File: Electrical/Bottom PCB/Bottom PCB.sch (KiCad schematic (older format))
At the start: 47 parts, among them J101 Steper1, J102 Steper2, J103 H Bridge, J104 Servo1, J105 Servo2, J106 Servo3, J107 Servo4, SW101 FL, SW102 FR, U101 ULN2003A, U102 74HC595, U103 QRE1113, U104 TB6612FNG, U105 74HC595, U106 QRE1113, U107 QRE1113, U108 MCP23017_SO, U109 QRE1113

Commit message: simplified the pcb,
Removed the shift registers and moved functionality onto the 16 way IO expander, also removed the H-Bridge, may re-add a I2C duel h-bridge at a later date.

Thinking about best way to drive the four servo headers, may use I2C controller for them as well, as then the timing maths is removed from the main micro
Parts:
- removed C105, C108: 100pF, Capacitor_SMD:C_1206_3216Metric_Pad1.42x1.75mm_HandSolder, symbol Device:C_Small
- removed C106: 10uF, Capacitor_SMD:C_1206_3216Metric_Pad1.42x1.75mm_HandSolder, symbol Device:C_Small
- removed J103: H Bridge, Connector_PinHeader_2.54mm:PinHeader_1x04_P2.54mm_Vertical, symbol Connector_Generic:Conn_01x04
- removed U102, U105: 74HC595, Package_SO:SOIC-16W_5.3x10.2mm_P1.27mm, symbol 74xx:74HC595
- removed U104: TB6612FNG, Package_SO:SSOP-24_5.3x8.2mm_P0.65mm, symbol Driver_Motor:TB6612FNG
- C102: value 100pF -> 10uF
- JP101, JP102, JP103: renamed from JP?; footprint (none) -> Jumper:SolderJumper-2_P1.3mm_Open_Pad1.0x1.5mm
- gave numbers to parts that had none: 3
- renumbered R109 to R112, R110 to R113, U108 to U107, U107 to U108
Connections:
- net labels removed: DATA, M1PWM, M2PWM, RCLK, SRCLK
- wire segments 262 -> 178
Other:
- moved on the sheet: C101, C102, C103, C104, J101, J102, JP101, JP102, JP103, R109, R110, R111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

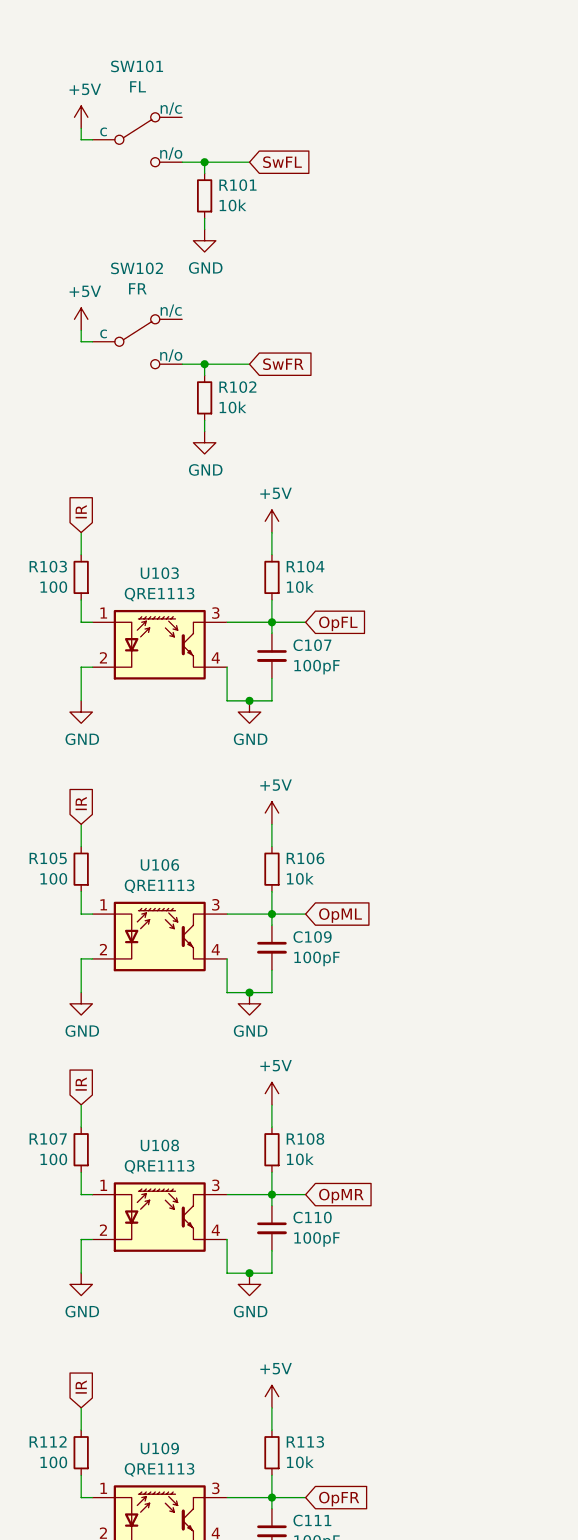
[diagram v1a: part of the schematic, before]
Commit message: moved some parts to 5V supply
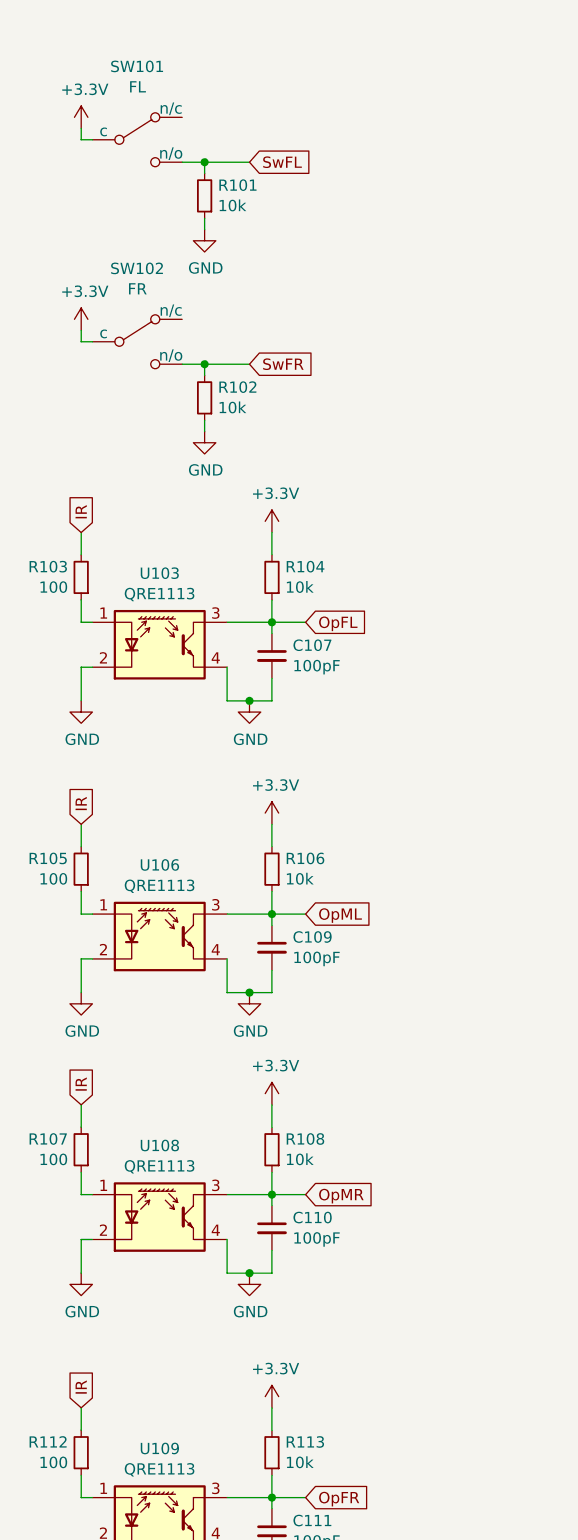
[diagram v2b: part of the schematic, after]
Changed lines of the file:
@@
-	1    0    0    -1
-$EndComp
-$Comp
-L power:+5V #PWR0115
-U 1 1 5DA4321E
-P 550 1650
-F 0 "#PWR0115" H 550 1500 50  0001 C CNN
-F 1 "+5V" H 565 1823 50  0000 C CNN
-F 2 "" H 550 1650 50  0001 C CNN
-F 3 "" H 550 1650 50  0001 C CNN
-	1    550  1650
 	1    0    0    -1
 $EndComp
@@
 F 3 "" H 1100 1200 50  0001 C CNN
 	1    1100 1200
-	1    0    0    -1
-$EndComp
-$Comp
-L power:+5V #PWR0106
-U 1 1 5DA58E34
-P 550 750
-F 0 "#PWR0106" H 550 600 50  0001 C CNN
-F 1 "+5V" H 565 923 50  0000 C CNN
-F 2 "" H 550 750 50  0001 C CNN
-F 3 "" H 550 750 50  0001 C CNN
-	1    550  750
 	1    0    0    -1
 $EndComp
@@
 	1    0    0    -1
 $EndComp
-$Comp
-L power:+5V #PWR0127
-U 1 1 5E63ABEC
-P 1400 2550
-F 0 "#PWR0127" H 1400 2400 50  0001 C CNN
-F 1 "+5V" H 1415 2723 50  0000 C CNN
-F 2 "" H 1400 2550 50  0001 C CNN
-F 3 "" H 1400 2550 50  0001 C CNN
-	1    1400 2550
-	1    0    0    -1
-$EndComp
 Wire Wire Line
 	550  2850 550  2950
@@
 	1    0    0    -1
 $EndComp
-$Comp
-L power:+5V #PWR0134
-U 1 1 5E7C0801
-P 1400 3850
-F 0 "#PWR0134" H 1400 3700 50  0001 C CNN
-F 1 "+5V" H 1415 4023 50  0000 C CNN
-F 2 "" H 1400 3850 50  0001 C CNN
-F 3 "" H 1400 3850 50  0001 C CNN
-	1    1400 3850
-	1    0    0    -1
-$EndComp
 Wire Wire Line
 	550  4150 550  4250
@@
 	1    0    0    -1
 $EndComp
-$Comp
-L power:+5V #PWR0145
-U 1 1 5E7D8F2B
-P 1400 5100
-F 0 "#PWR0145" H 1400 4950 50  0001 C CNN
-F 1 "+5V" H 1415 5273 50  0000 C CNN
-F 2 "" H 1400 5100 50  0001 C CNN
-F 3 "" H 1400 5100 50  0001 C CNN
-	1    1400 5100
-	1    0    0    -1
-$EndComp
 Wire Wire Line
 	550  5400 550  5500
@@
 Wire Wire Line
 	550  6750 550  6850
-$Comp
-L power:+5V #PWR0149
-U 1 1 5E7513F0
-P 1400 6450
-F 0 "#PWR0149" H 1400 6300 50  0001 C CNN
-F 1 "+5V" H 1415 6623 50  0000 C CNN
-F 2 "" H 1400 6450 50  0001 C CNN
-F 3 "" H 1400 6450 50  0001 C CNN
-	1    1400 6450
-	1    0    0    -1
-$EndComp
 $Comp
 L Device:C_Small C111
@@
 	5200 2400 5650 2400
 $Comp
-L power:+5V #PWR?
+L power:+5V #PWR0102
 U 1 1 5EE845C0
 P 6950 4900
-F 0 "#PWR?" H 6950 4750 50  0001 C CNN
+F 0 "#PWR0102" H 6950 4750 50  0001 C CNN
 F 1 "+5V" H 6965 5073 50  0000 C CNN
 F 2 "" H 6950 4900 50  0001 C CNN
@@
 	1    0    0    -1
 $EndComp
+$Comp
+L power:+3.3V #PWR?
+U 1 1 5EBBD63B
+P 550 750
+AR Path="/5EBBD63B" Ref="#PWR?"  Part="1"
+AR Path="/5EBB31C5/5EBBD63B" Ref="#PWR?"  Part="1"
+F 0 "#PWR?" H 550 600 50  0001 C CNN
+F 1 "+3.3V" H 565 923 50  0000 C CNN
+F 2 "" H 550 750 50  0001 C CNN
+F 3 "" H 550 750 50  0001 C CNN
+	1    550  750
+	1    0    0    -1
+$EndComp
+$Comp
+L power:+3.3V #PWR?
+U 1 1 5EBBDE12
+P 550 1650
+AR Path="/5EBBDE12" Ref="#PWR?"  Part="1"
+AR Path="/5EBB31C5/5EBBDE12" Ref="#PWR?"  Part="1"
+F 0 "#PWR?" H 550 1500 50  0001 C CNN
+F 1 "+3.3V" H 565 1823 50  0000 C CNN
+F 2 "" H 550 1650 50  0001 C CNN
+F 3 "" H 550 1650 50  0001 C CNN
+	1    550  1650
+	1    0    0    -1
+$EndComp
+$Comp
+L power:+3.3V #PWR?
+U 1 1 5EBBE41D
+P 1400 2550
+AR Path="/5EBBE41D" Ref="#PWR?"  Part="1"
+AR Path="/5EBB31C5/5EBBE41D" Ref="#PWR?"  Part="1"
+F 0 "#PWR?" H 1400 2400 50  0001 C CNN
+F 1 "+3.3V" H 1415 2723 50  0000 C CNN
+F 2 "" H 1400 2550 50  0001 C CNN
+F 3 "" H 1400 2550 50  0001 C CNN
+	1    1400 2550
+	1    0    0    -1
+$EndComp
+$Comp
+L power:+3.3V #PWR?
+U 1 1 5EBBEC39
+P 1400 3850
+AR Path="/5EBBEC39" Ref="#PWR?"  Part="1"
+AR Path="/5EBB31C5/5EBBEC39" Ref="#PWR?"  Part="1"
+F 0 "#PWR?" H 1400 3700 50  0001 C CNN
+F 1 "+3.3V" H 1415 4023 50  0000 C CNN
+F 2 "" H 1400 3850 50  0001 C CNN
+F 3 "" H 1400 3850 50  0001 C CNN
+	1    1400 3850
+	1    0    0    -1
+$EndComp
+$Comp
+L power:+3.3V #PWR?
+U 1 1 5EBBF53B
+P 1400 5100
+AR Path="/5EBBF53B" Ref="#PWR?"  Part="1"
+AR Path="/5EBB31C5/5EBBF53B" Ref="#PWR?"  Part="1"
+F 0 "#PWR?" H 1400 4950 50  0001 C CNN
+F 1 "+3.3V" H 1415 5273 50  0000 C CNN
+F 2 "" H 1400 5100 50  0001 C CNN
+F 3 "" H 1400 5100 50  0001 C CNN
+	1    1400 5100
+	1    0    0    -1
+$EndComp
+$Comp
+L power:+3.3V #PWR?
+U 1 1 5EBBFB46
+P 1400 6450
+AR Path="/5EBBFB46" Ref="#PWR?"  Part="1"
+AR Path="/5EBB31C5/5EBBFB46" Ref="#PWR?"  Part="1"
+F 0 "#PWR?" H 1400 6300 50  0001 C CNN
+F 1 "+3.3V" H 1415 6623 50  0000 C CNN
+F 2 "" H 1400 6450 50  0001 C CNN
+F 3 "" H 1400 6450 50  0001 C CNN
+	1    1400 6450
+	1    0    0    -1
+$EndComp

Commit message: removed the servos at the moment
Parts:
- removed J104: Servo1, Connector_PinHeader_2.54mm:PinHeader_1x03_P2.54mm_Vertical, symbol Connector_Generic:Conn_01x03
- removed J105: Servo2, Connector_PinHeader_2.54mm:PinHeader_1x03_P2.54mm_Vertical, symbol Connector_Generic:Conn_01x03
- removed J106: Servo3, Connector_PinHeader_2.54mm:PinHeader_1x03_P2.54mm_Vertical, symbol Connector_Generic:Conn_01x03
- removed J107: Servo4, Connector_PinHeader_2.54mm:PinHeader_1x03_P2.54mm_Vertical, symbol Connector_Generic:Conn_01x03
- renumbered C107 to C103, C103 to C104, C104 to C105, C109 to C106, C110 to C107, C111 to C108, R109 to R105, R110 to R106, R111 to R107, R105 to R108, R106 to R109, R107 to R110, R108 to R111, U103 to U102, U107 to U103, U106 to U104, U108 to U105, U109 to U106
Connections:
- net labels removed: Servo1, Servo2, Servo3, Servo4
- wire segments 178 -> 158
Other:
- moved on the sheet: C101, C102, C104, C105, HC-SR101, J101, J102, JP101, JP102, JP103, R105, R106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

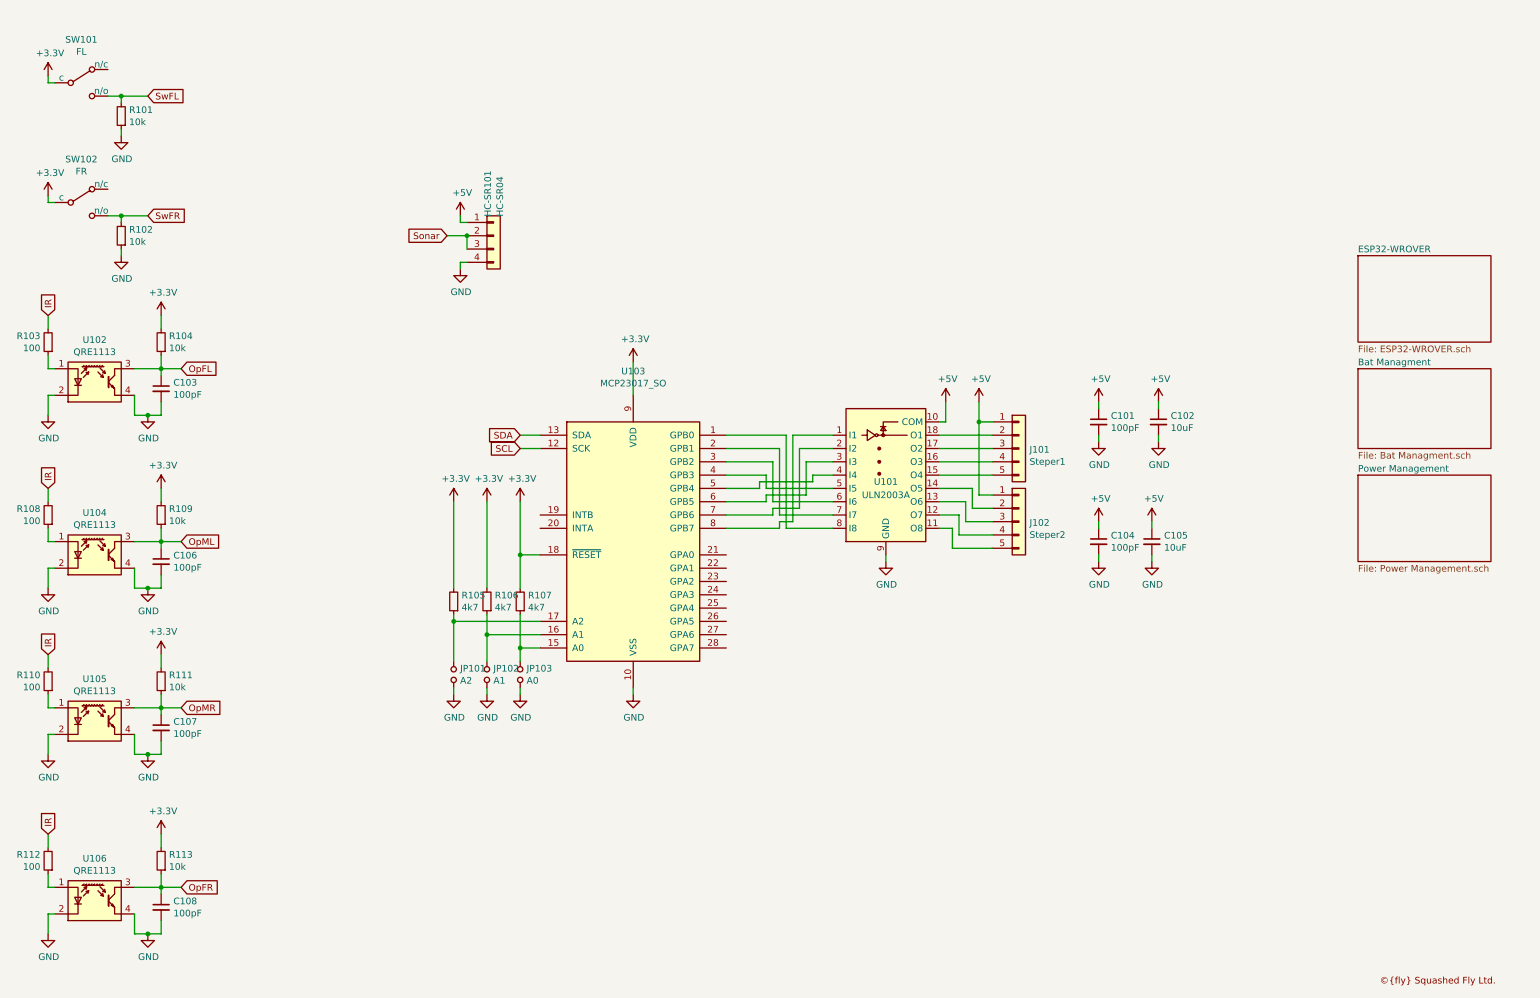
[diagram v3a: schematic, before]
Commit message: Added power switch
Some more modifications
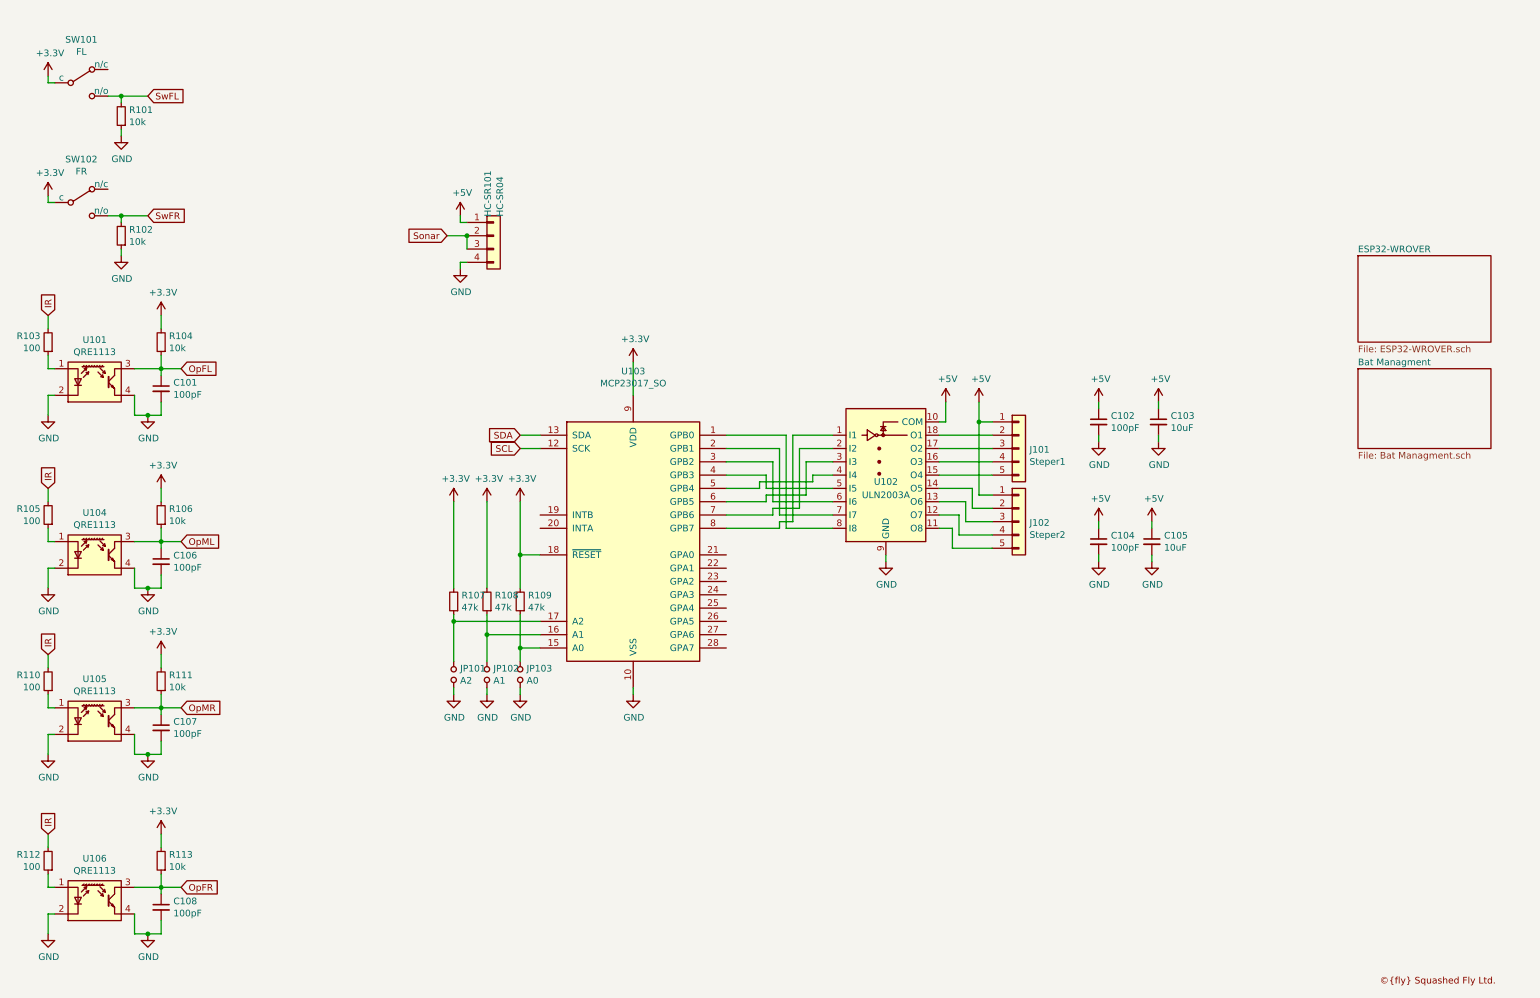
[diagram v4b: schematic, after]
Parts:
- R107: renamed from R105; value 4k7 -> 47k
- R108: renamed from R106; value 4k7 -> 47k
- R109: renamed from R107; value 4k7 -> 47k
- renumbered C103 to C101, C101 to C102, C102 to C103, R108 to R105, R109 to R106, U102 to U101, U101 to U102

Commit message: added more stuff
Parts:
- added R102: 2k7, Resistor_SMD:R_1206_3216Metric_Pad1.42x1.75mm_HandSolder, symbol Device:R_Small
- added R103: 4k7, Resistor_SMD:R_1206_3216Metric_Pad1.42x1.75mm_HandSolder, symbol Device:R_Small
- renumbered R102 to R104, R103 to R105, R104 to R106, R105 to R107, R106 to R108, R107 to R109, R108 to R110, R109 to R111, R110 to R112, R111 to R113, R112 to R114, R113 to R115
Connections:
- net GND: now also R103.2
- net Sonar: no longer names the net of HC-SR101.3 (Pin_3)
- net Sonar: now also R102.2; no longer HC-SR101.2 (Pin_2)
- new net Sonar_Echo: R102.1, R103.1
- new net Sonar_Trig: HC-SR101.2 (Pin_2)
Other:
- moved on the sheet: HC-SR101, JP101, JP102, R109, R110
